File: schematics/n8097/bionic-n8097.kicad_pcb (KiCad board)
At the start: 2 copper layers, 31.8 x 68.6 mm, 8 parts, among them J1 Bionic-P135, J2 Bionic-P245, U1 N8095BH, U2 11AA010-I/TT

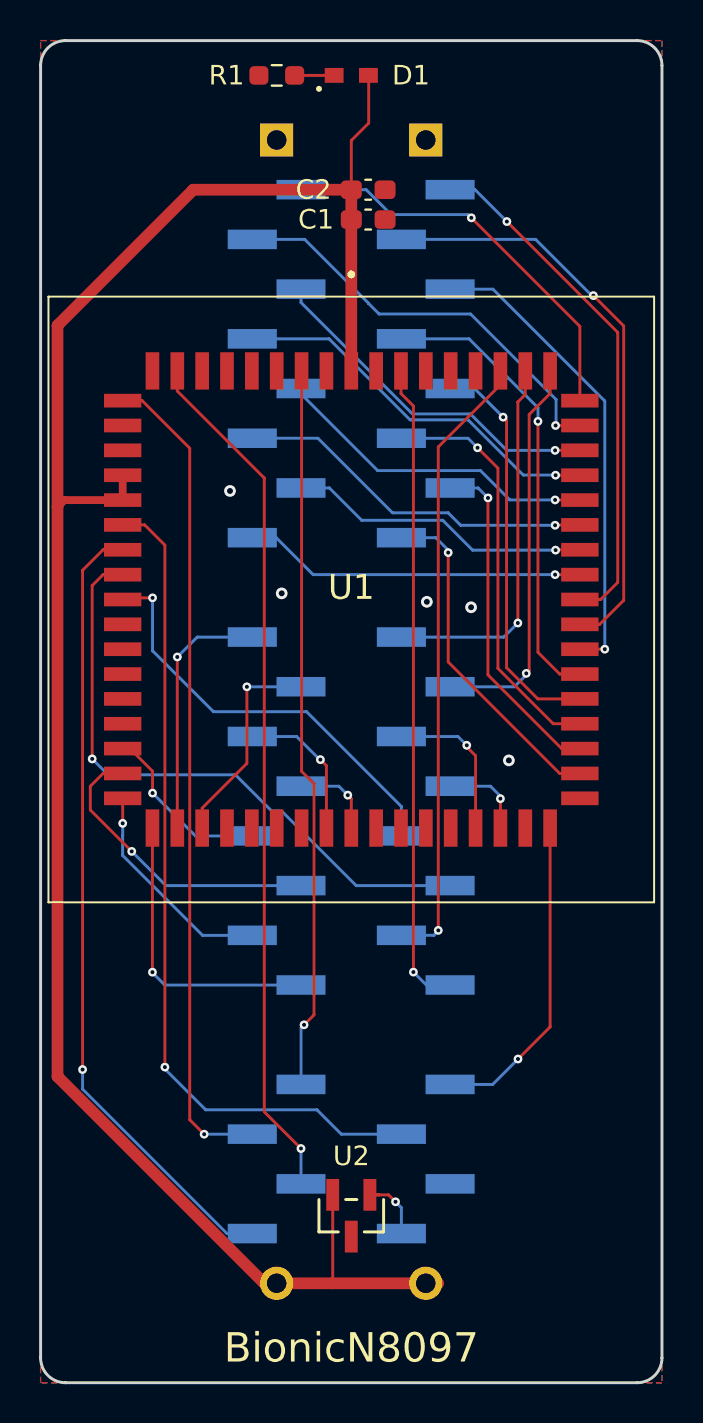
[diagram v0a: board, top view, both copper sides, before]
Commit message: [schematics] Straighten board tracks and regenerate Gerbers
straighten_tracks.py on every routed board: router leftovers snapped to
0/45/90 degrees and redundant segments merged, each pass DRC-checked
(counts unchanged). Gerbers and drill files of the changed boards are
regenerated with each board's plot settings, keeping the committed file
sets; tms9980 keeps its tracks (the rebuild left a dangling VCC stub).
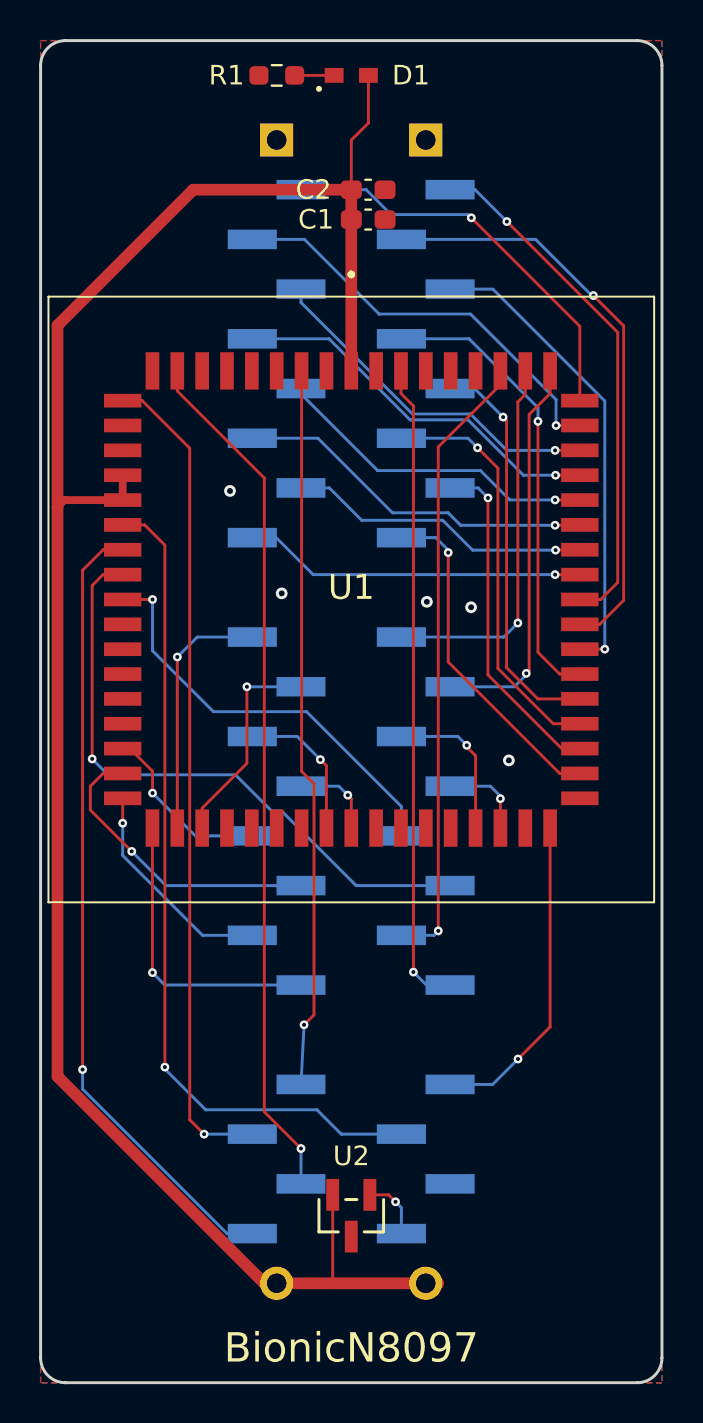
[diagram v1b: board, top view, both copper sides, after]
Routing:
- net INST: track 32.5 -> 31.2 mm
- net AD12: track 20.6 -> 19.3 mm
- net AD7: track 17.5 -> 16.3 mm
- net XTAL1: track 33.1 -> 31.9 mm
- net Net-(J2-P57): track 4.37 -> 3.21 mm
- net AD14: track 17.4 -> 16.5 mm
- net AD8: track 27.3 -> 26.7 mm
- net AD9: track 30.6 -> 30.0 mm
- net ~{RESET}: track 41.4 -> 40.7 mm

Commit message: [schematics] Align silkscreen reference labels
align_silk.py snaps each footprint kind's labels onto their common
offset and angle and clears labels DRC flags on silkscreen; 76 labels on
22 boards, no DRC count grows. Their Gerbers are regenerated.
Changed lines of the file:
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@@
 		(tags "capacitor handsolder")
 		(property "Reference" "C1"
-			(at -2.667 -0.0019 0)
+			(at -2.73 0 0)
 			(layer "F.SilkS")
 			(effects
@@
 		(tags "capacitor handsolder")
 		(property "Reference" "C2"
-			(at -2.794 0 0)
-			(layer "F.SilkS")
-			(effects
+			(at -2.73 0 0)
+			(layer "F.SilkS")
+			(effects

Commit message: [schematics] Remove the JLC order-number marker from all boards
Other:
- board text removed: "JLCJLCJLCJLC"
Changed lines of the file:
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@@
-		)
-	)
-	(gr_text "JLCJLCJLCJLC"
-		(at 116.875 137.818 -0)
-		(layer "B.SilkS")
-		(effects
-			(font
-				(size 0.8 0.8)
-				(thickness 0.1)
-			)
-			(justify bottom mirror)
 		)
 	)
